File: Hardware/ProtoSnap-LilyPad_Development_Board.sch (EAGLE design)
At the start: 140 parts, among them M1 VIBE MOTOR, U1 ATMEGA328, U2 MCP9700, U4 MCP73831, U6 LIGHTSENSOR_ALS-PT19, Y1 8MHz

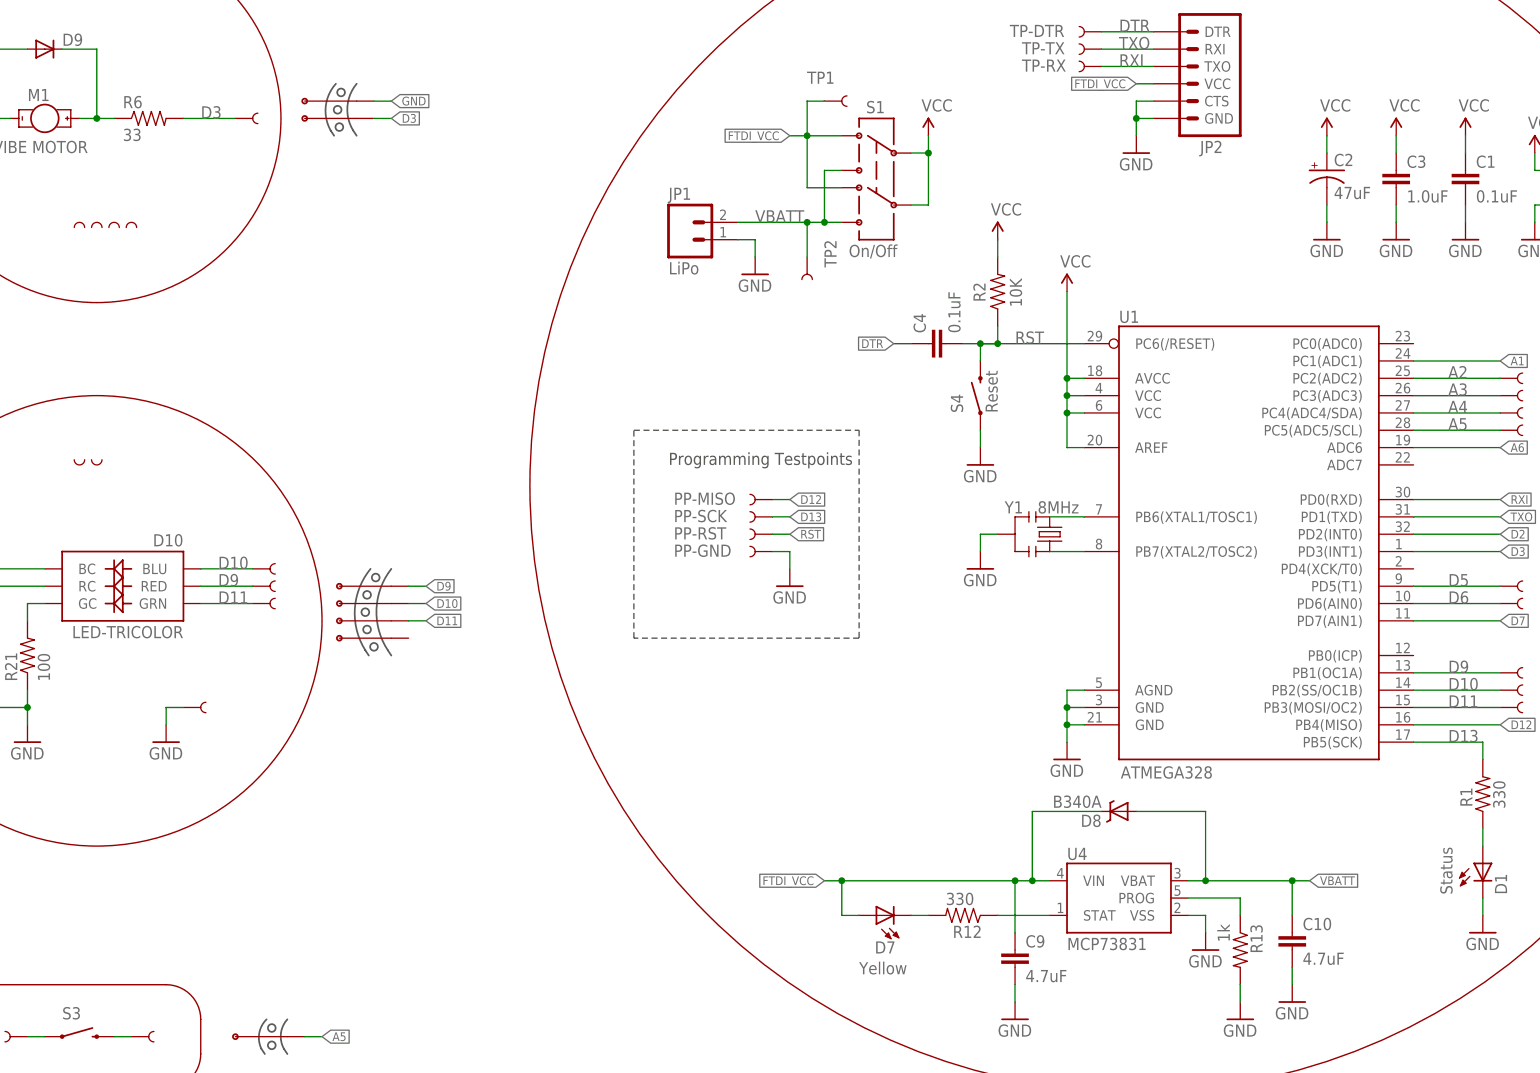
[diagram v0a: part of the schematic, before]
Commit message: Adding Prod IDs (not 100% done)
Also had to reroute traces off of IC
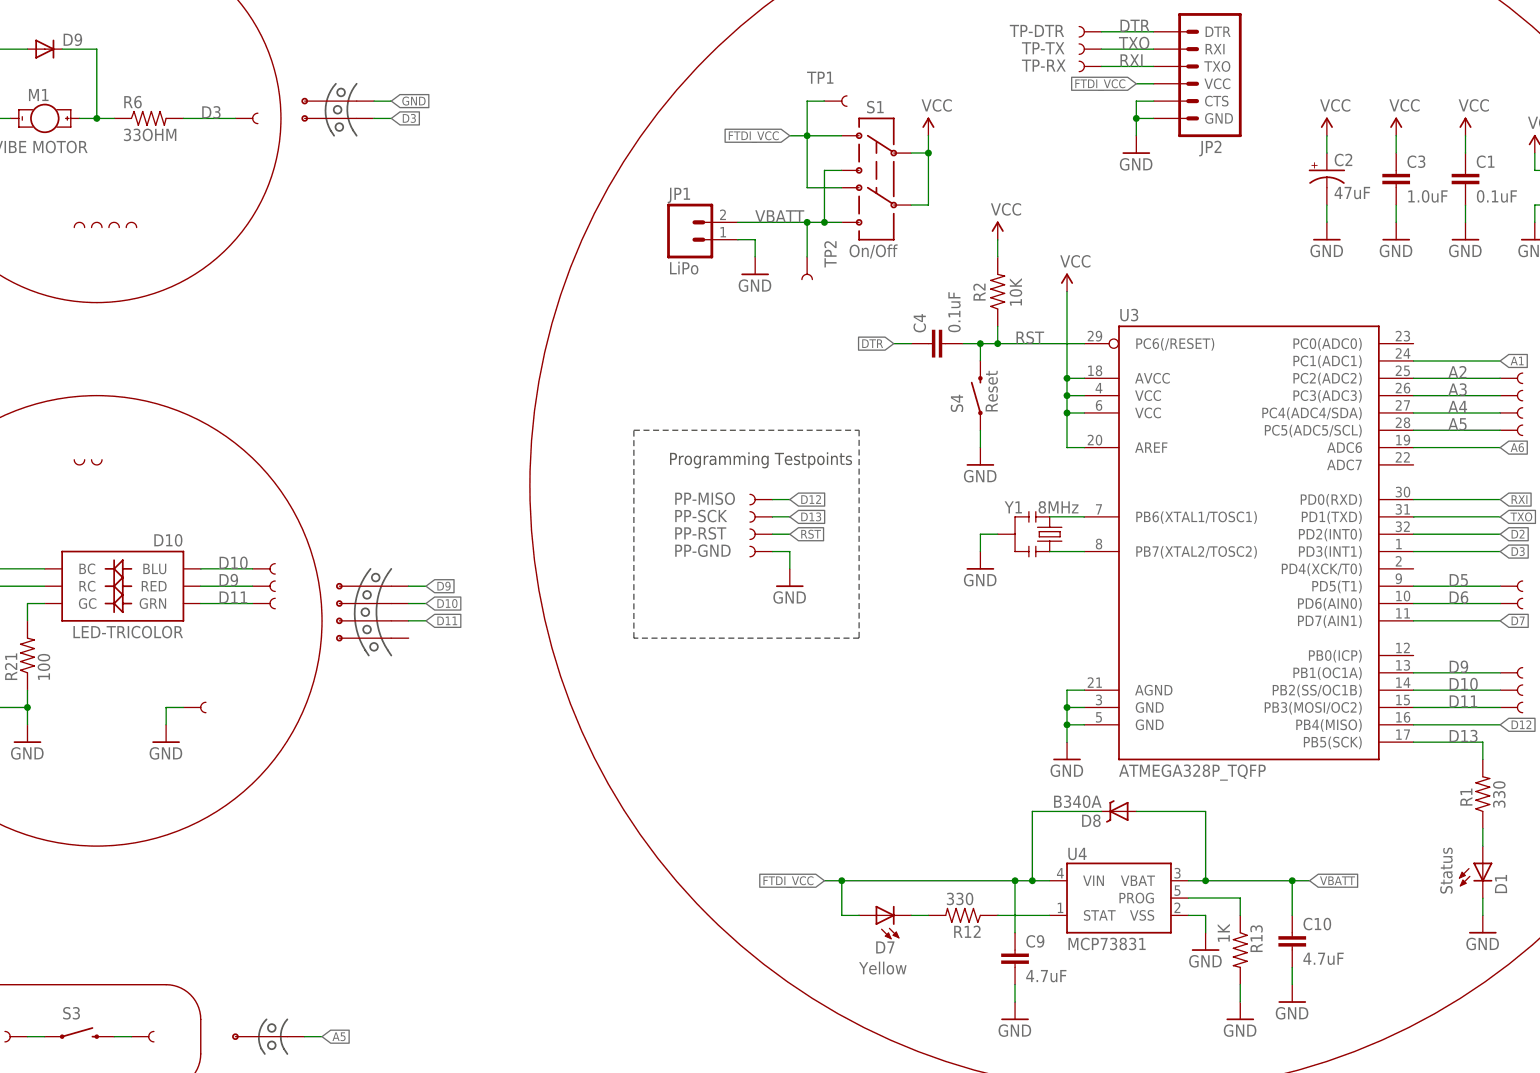
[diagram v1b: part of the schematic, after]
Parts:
- removed U1: ATMEGA328, SparkFun:ATMEGA168
- added U3: ATMEGA328P_TQFP, SparkFun-DigitalIC:ATMEGA328P_TQFP
- B1: device SparkFun:BUZZERSMD2 -> SparkFun-Electromechanical:BUZZERSMD2
- C1, C4: device SparkFun:CAP0603-CAP -> SparkFun-Capacitors:0.1UF-25V(+80/-20%)(0603)
- C10, C9: device SparkFun:CAP0603-CAP -> SparkFun-Capacitors:4.7UF-6.3V-10%(0603)0603
- C2: device SparkFun:CAP_POL3528 -> SparkFun-Capacitors:47UF-10V-10%(TANT)
- C3: device SparkFun:CAP0603-CAP -> SparkFun-Capacitors:1.0UF-16V-10%(0603)
- R, R10, R11, R8, R9: device SparkFun:RESISTOR0603-RES -> SparkFun-Resistors:100OHM-1/10W-1%(0603)
- R1, R12: device SparkFun:RESISTOR0603-RES -> SparkFun-Resistors:330OHM1/10W1%(0603)
- R13: value 1k -> 1K; device SparkFun:RESISTOR0603-RES -> SparkFun-Resistors:1KOHM-1/10W-1%(0603)
- R19, R21: device SparkFun-Resistors:100OHM1/10W1%(0603) -> SparkFun-Resistors:100OHM-1/10W-1%(0603)
- R2, R7: device SparkFun:RESISTOR0603-RES -> SparkFun-Resistors:10KOHM-1/10W-1%(0603)0603
- R6: value 33 -> 33OHM; device SparkFun:RESISTOR0603-RES -> SparkFun-Resistors:33OHM1/10W1%(0603)
- U2: device SparkFun:MCP9700SMD -> SparkFun-Sensors:MCP9700SMD
- U4: device SparkFun:MCP73831 -> SparkFun-PowerIC:MCP73831
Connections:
- net A1: now also U3.PC1(ADC1); no longer U1.PC1(ADC1)
- net A2: now also U3.PC2(ADC2); no longer U1.PC2(ADC2)
- net A3: now also U3.PC3(ADC3); no longer U1.PC3(ADC3)
- net A4: now also U3.PC4(ADC4/SDA); no longer U1.PC4(ADC4/SDA)
- net A5: now also U3.PC5(ADC5/SCL); no longer U1.PC5(ADC5/SCL)
- net A6: now also U3.ADC6; no longer U1.ADC6
- net D10: now also U3.PB2(SS/OC1B); no longer U1.PB2(SS/OC1B)
- net D11: now also U3.PB3(MOSI/OC2); no longer U1.PB3(MOSI/OC2)
- net D12: now also U3.PB4(MISO); no longer U1.PB4(MISO)
- net D13: now also U3.PB5(SCK); no longer U1.PB5(SCK)
- net D2: now also U3.PD2(INT0); no longer U1.PD2(INT0)
- net D3: now also U3.PD3(INT1); no longer U1.PD3(INT1)
- net D5: now also U3.PD5(T1); no longer U1.PD5(T1)
- net D6: now also U3.PD6(AIN0); no longer U1.PD6(AIN0)
- net D7: now also U3.PD7(AIN1); no longer U1.PD7(AIN1)
- net D9: now also U3.PB1(OC1A); no longer U1.PB1(OC1A)
- net GND: now also U3.AGND, U3.GND@3, U3.GND@5; no longer U1.AGND, U1.GND@1, U1.GND@2
- net N$1: now also U3.PB6(XTAL1/TOSC1); no longer U1.PB6(XTAL1/TOSC1)
- net N$3: now also U3.PB7(XTAL2/TOSC2); no longer U1.PB7(XTAL2/TOSC2)
- net RST: now also U3.PC6(/RESET); no longer U1.PC6(/RESET)
- net RXI: now also U3.PD0(RXD); no longer U1.PD0(RXD)
- net TXO: now also U3.PD1(TXD); no longer U1.PD1(TXD)
- net VCC: now also U3.AREF, U3.AVCC, U3.VCC@4, U3.VCC@6; no longer U1.AREF, U1.AVCC, U1.VCC@1, U1.VCC@2

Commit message: More schematic cleanup
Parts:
- M1: value VIBE MOTOR -> VIBE
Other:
- moved on the sheet: C1, C10, C2, C3, C4, C9, D1, D2, D3, D5, D6, D7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

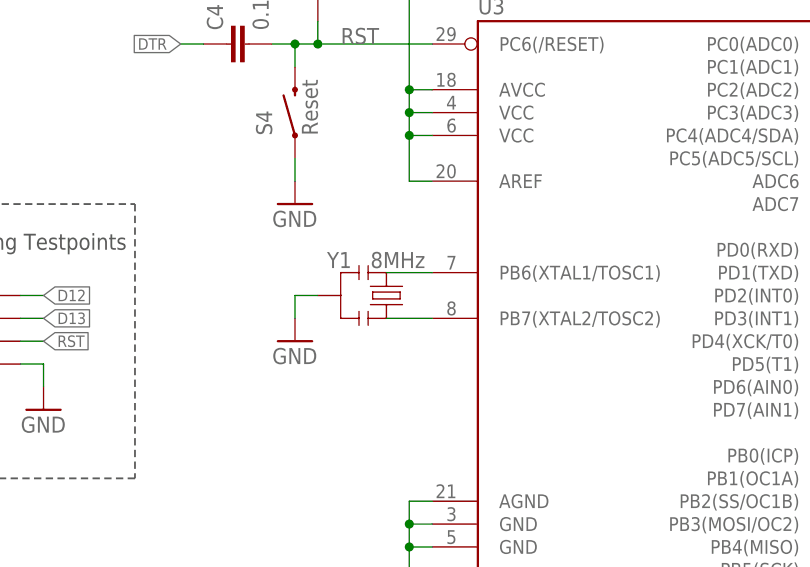
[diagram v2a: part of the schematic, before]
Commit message: fixing some acid traps and scooting some component
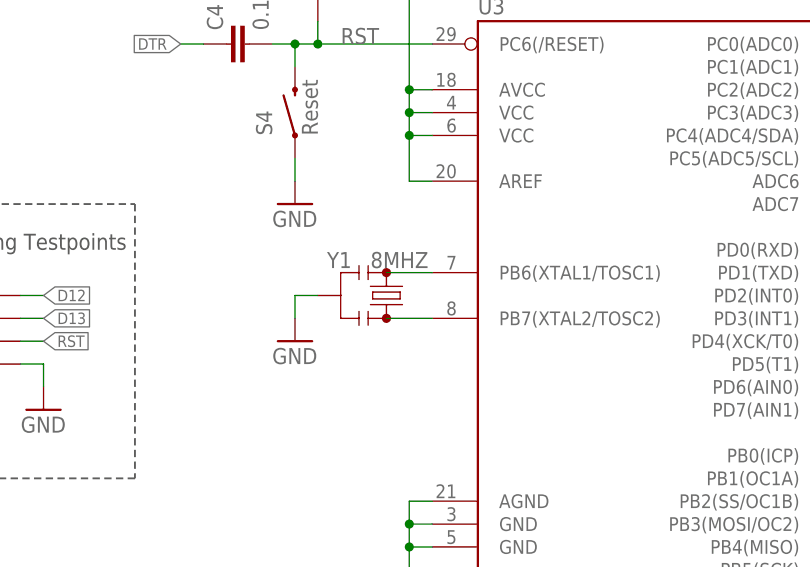
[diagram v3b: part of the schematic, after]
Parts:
- Y1: value 8MHz -> 8MHZ
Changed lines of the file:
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@@
 <part name="GND3" library="SparkFun" deviceset="GND" device=""/>
 <part name="GND4" library="SparkFun" deviceset="GND" device=""/>
-<part name="Y1" library="SparkFun-FreqCtrl" deviceset="RESONATOR" device="8MHZ" value="8MHz"/>
+<part name="Y1" library="SparkFun-FreqCtrl" deviceset="RESONATOR" device="8MHZ" value="8MHZ"/>
 <part name="GND9" library="SparkFun" deviceset="GND" device=""/>
 <part name="JP2" library="SparkFun" deviceset="ARDUINO_SERIAL_PROGRAM" device="SMD"/>
